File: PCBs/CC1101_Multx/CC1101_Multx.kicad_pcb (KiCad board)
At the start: 4 copper layers, 41 x 26.6 mm, 45 parts, among them IC1 CC1101RGPR, IC2 ASWD-S2-0005-T, IC3 ASWD-S2-0005-T, IC4 ASWD-S2-0005-T, J1 MCU, J2 MCU, J3 MCU, J4 MCU, J5 MCU, J6 MCU, J7 MCU, J8 MCU, J9 MCU, Y1 XRCGB26M000F1S2BR0

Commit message: layout2
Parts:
- added REF**: MountingHole_2.2mm_M2_DIN965, MountingHole:MountingHole_2.2mm_M2_DIN965, F.Cu at (152.4, 89.5)
- added REF**: MountingHole_2.2mm_M2_DIN965, MountingHole:MountingHole_2.2mm_M2_DIN965, F.Cu at (152.4, 71.5)
- added REF**: MountingHole_2.2mm_M2_DIN965, MountingHole:MountingHole_2.2mm_M2_DIN965, F.Cu at (175.1, 89.5)
- added REF**: MountingHole_2.2mm_M2_DIN965, MountingHole:MountingHole_2.2mm_M2_DIN965, F.Cu at (175.8, 71.5)
- moved BT1 2.65 mm to (159.2, 73.1)
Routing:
- net Net-(IC4-VCTL): track 45.8 -> 40.0 mm
- net Net-(IC2-VCTL): track 27.2 -> 29.2 mm
- net /AGND: track 25.7 -> 26.0 mm, vias 12 -> 119
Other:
- board size 41 x 26.6 mm -> 41.1 x 26.8 mm

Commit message: Layout V
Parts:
- moved AE1 0.12 mm to (182.2, 83.4)
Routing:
- net Net-(IC1-SCLK): track 8.63 -> 7.24 mm
- net /AGND: vias 119 -> 175

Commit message: BOM 1
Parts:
- AE1: footprint Connector_Coaxial:SMA_Molex_73251-1153_EdgeMount_Horizontal -> Connector_Coaxial:SMA_Molex_73251-2120_EdgeMount_Horizontal
- moved AE1 1.54 mm to (183.7, 83.4), turned to 0 degrees
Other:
- board size 41.1 x 26.8 mm -> 39.6 x 26.8 mm

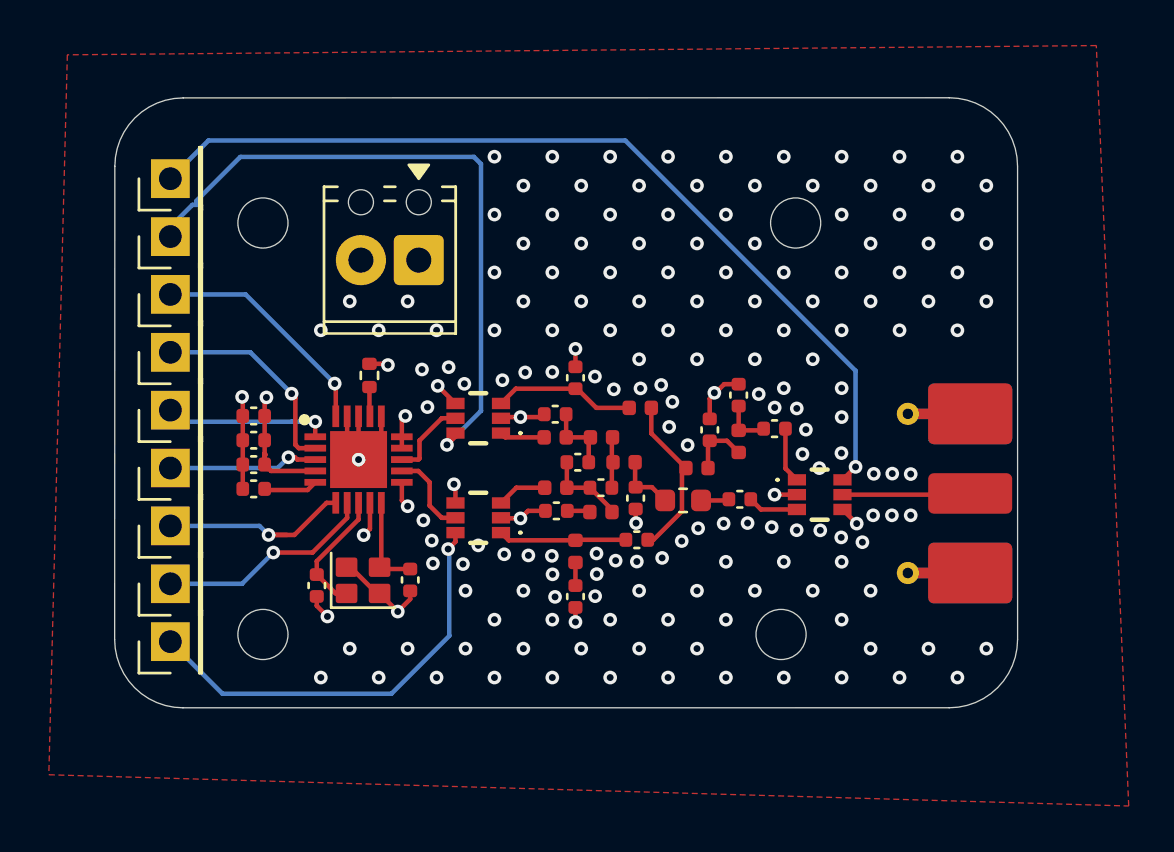
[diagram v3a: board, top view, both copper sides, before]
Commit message: Layout new switch and BOM
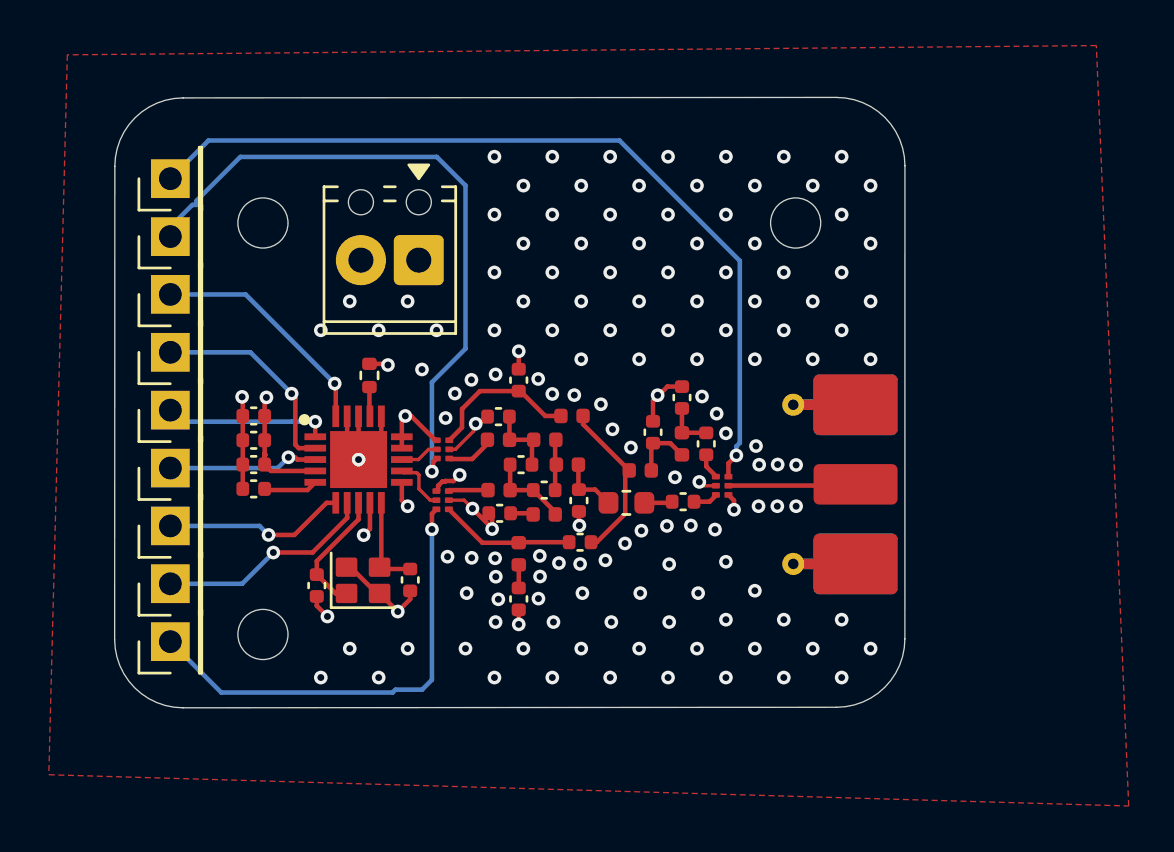
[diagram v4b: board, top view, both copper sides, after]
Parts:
- removed the REF** at (175.1, 89.5)
- C51: value 100n -> 100nF
- IC2, IC3, IC4: footprint Library:ASWDS20005T -> Library:ASWS_S2_0002
- moved AE1 5.05 mm to (178.7, 83.0)
- moved IC4 4.13 mm to (172.8, 82.6), turned to 0 degrees
- moved C125_1 3.07 mm to (171.9, 81.2), turned to 90 degrees
- moved L131_1 3.02 mm to (166.0, 80.0)
- moved IC2 2.50 mm to (160.1, 81.8), turned to 180 degrees
- moved C124_1 2.49 mm to (163.6, 88.0)
- moved C124_2 2.49 mm to (162.8, 84.2)
- moved C131_1 2.49 mm to (163.6, 78.4)
- moved L121_1 2.49 mm to (163.6, 86.0)
- moved C122_1 2.49 mm to (169.5, 80.7)
- moved C123_1 2.49 mm to (170.8, 79.2)
- moved C125_2 2.49 mm to (170.8, 83.7)
- moved C131_2 2.49 mm to (162.7, 80.0)
- moved L122_1 2.49 mm to (169.0, 82.4)
- moved L124_2 2.49 mm to (168.4, 83.8)
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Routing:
- net Net-(IC4-VCTL): track 40.0 -> 37.5 mm
- net /RF_N: track 3.56 -> 1.72 mm
- net /AGND: track 26.0 -> 27.8 mm, vias 175 -> 142
- net /RF_P: track 3.81 -> 2.40 mm
- net /433_A: track 2.45 -> 1.11 mm
- net Net-(IC3-VCTL): track 18.9 -> 20.2 mm
- net /AVDD: track 12.9 -> 14.0 mm, vias 7 -> 6
- net /868_A: track 2.21 -> 1.07 mm
- net Net-(IC1-GDO0_(ATEST)): track 8.82 -> 8.01 mm
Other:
- board size 39.6 x 26.8 mm -> 34.7 x 26.8 mm

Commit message: BOM e tudo mais
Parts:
- added REF**: MountingHole_2.2mm_M2_DIN965, MountingHole:MountingHole_2.2mm_M2_DIN965, F.Cu at (167.1, 89.5)
- moved REF** 8.64 mm to (167.1, 71.5)
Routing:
- net /AGND: vias 142 -> 139
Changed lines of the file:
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@@
 			(outputformat 1)
 			(mirror no)
-			(drillshape 1)
+			(drillshape 0)
 			(scaleselection 1)
-			(outputdirectory "")
+			(outputdirectory "Gerbers/")
 		)
 	)
@@
 		(embedded_fonts no)
 	)
+	(footprint "MountingHole:MountingHole_2.2mm_M2_DIN965"
+		(layer "F.Cu")
+		(at 167.135534 89.55)
+		(descr "Mounting Hole 2.2mm, M2, no annular, generated by kicad-footprint-generator mountinghole.py")
+		(tags "mountinghole M2 DIN965")
+		(property "Reference" "REF**"
+			(at 0 -2.85 0)
+			(layer "F.SilkS")
+			(hide yes)
+			(effects
+				(font
+					(size 1 1)
+					(thickness 0.15)
+				)
+			)
+		)
+		(property "Value" "MountingHole_2.2mm_M2_DIN965"
+			(at 0 2.85 0)
+			(layer "F.Fab")
+			(hide yes)
+			(effects
+				(font
+					(size 1 1)
+					(thickness 0.15)
+				)
+			)
+		)
+		(property "Datasheet" ""
+			(at 0 0 0)
+			(layer "F.Fab")
+			(hide yes)
+			(effects
+				(font
+					(size 1.27 1.27)
+				)
+			)
+		)
+		(property "Description" ""
+			(at 0 0 0)
+			(layer "F.Fab")
+			(hide yes)
+			(effects
+				(font
+					(size 1.27 1.27)
+				)
+			)
+		)
+		(property "KiLib_Generator" "mounting_hardware/mounting_hole"
+			(at 0 0 0)
+			(layer "F.SilkS")
+			(hide yes)
+			(effects
+				(font
+					(size 1 1)
+					(thickness 0.15)
+				)
+			)
+		)
+		(attr exclude_from_pos_files exclude_from_bom)
+		(duplicate_pad_numbers_are_jumpers no)
+		(fp_circle
+			(center 0 0)
+			(end 1.9 0)
+			(stroke
+				(width 0.15)
+				(type solid)
+			)
+			(fill no)
+			(layer "Cmts.User")
+		)
+		(fp_circle
+			(center 0 0)
+			(end 2.15 0)
+			(stroke
+				(width 0.05)
+				(type solid)
+			)
+			(fill no)
+			(layer "F.CrtYd")
+		)
+		(pad "" np_thru_hole circle
+			(at 0 0)
+			(size 2.2 2.2)
+			(drill 2.2)
+			(layers "*.Cu" "*.Mask")
+		)
+		(embedded_fonts no)
+	)
 	(footprint "Capacitor_SMD:C_0402_1005Metric"
 		(layer "F.Cu")
@@
 	(footprint "MountingHole:MountingHole_2.2mm_M2_DIN965"
 		(layer "F.Cu")
-		(at 175.78 71.49)
+		(at 167.135534 71.484449)
 		(descr "Mounting Hole 2.2mm, M2, no annular, generated by kicad-footprint-generator mountinghole.py")
 		(tags "mountinghole M2 DIN965")
@@
 	)
 	(via
+		(at 167.64 73.66)
+		(size 0.6)
+		(drill 0.3)
+		(layers "F.Cu" "B.Cu")
+		(free yes)
+		(net "/AGND")
+	)
+	(via
 		(at 161.340794 87.7359)
 		(size 0.6)
@@
 	)
 	(via
+		(at 175.26 71.12)
+		(size 0.6)
+		(drill 0.3)
+		(layers "F.Cu" "B.Cu")
+		(free yes)
+		(net "/AGND")
+	)
+	(via
 		(at 171.500794 87.7359)
 		(size 0.6)
@@
 	)
 	(via
-		(at 168.91 90.17)
-		(size 0.6)
-		(drill 0.3)
-		(layers "F.Cu" "B.Cu")
-		(free yes)
-		(net "/AGND")
-	)
-	(via
 		(at 175.800792 82.1107)
 		(size 0.6)
@@
 	)
 	(via
+		(at 165.1 73.66)
+		(size 0.6)
+		(drill 0.3)
+		(layers "F.Cu" "B.Cu")
+		(free yes)
+		(net "/AGND")
+	)
+	(via
 		(at 173.99 72.39)
 		(size 0.6)
@@
 	)
 	(via
-		(at 165.150794 89.0059)
+		(at 176.53 72.39)
 		(size 0.6)
 		(drill 0.3)
@@
 	)
 	(via
-		(at 165.1 71.12)
-		(size 0.6)
-		(drill 0.3)
-		(layers "F.Cu" "B.Cu")
-		(net "/AGND")
-	)
-	(via
 		(at 167.64 76.2)
 		(size 0.6)
@@
 	)
 	(via
-		(at 168.91 72.39)
+		(at 177.8 88.9)
 		(size 0.6)
 		(drill 0.3)
 		(layers "F.Cu" "B.Cu")
+		(free yes)
 		(net "/AGND")
 	)
 	(via
-		(at 177.8 88.9)
+		(at 165.1 71.12)
 		(size 0.6)
 		(drill 0.3)
@@
 	)
 	(via
-		(at 167.64 73.66)
+		(at 161.29 90.17)
 		(size 0.6)
 		(drill 0.3)
 		(layers "F.Cu" "B.Cu")
+		(free yes)
 		(net "/AGND")
 	)
 	(via
-		(at 161.29 90.17)
+		(at 158.75 90.17)
 		(size 0.6)
 		(drill 0.3)
@@
 	)
 	(via
-		(at 158.75 90.17)
+		(at 173.99 87.63)
 		(size 0.6)
 		(drill 0.3)
@@
 	)
 	(via
-		(at 173.99 87.63)
+		(at 168.91 72.39)
 		(size 0.6)
 		(drill 0.3)
@@
 	)
 	(via
+		(at 166.37 74.93)
+		(size 0.6)
+		(drill 0.3)
+		(layers "F.Cu" "B.Cu")
+		(free yes)
+		(net "/AGND")
+	)
+	(via
 		(at 171.45 74.93)
 		(size 0.6)
@@
 	)
 	(via
-		(at 166.37 90.17)
+		(at 166.37 69.85)
 		(size 0.6)
 		(drill 0.3)
@@
 	)
 	(via
-		(at 173.99 77.47)
+		(at 166.37 87.63)
 		(size 0.6)
 		(drill 0.3)
@@
 	)
 	(via
-		(at 159.38 77.92)
-		(size 0.6)
-		(drill 0.3)
-		(layers "F.Cu" "B.Cu")
-		(net "/AGND")
-	)
-	(via
-		(at 169.010794 84.9959)
-		(size 0.6)
-		(drill 0.3)
-		(layers "F.Cu" "B.Cu")
-		(net "/AGND")
-	)
-	(via
-		(at 172.72 76.2)
+		(at 173.99 77.47)
 		(size 0.6)
 		(drill 0.3)
 		(layers "F.Cu" "B.Cu")
+		(free yes)
 		(net "/AGND")
 	)
 	(via
-		(at 165.1 73.66)
+		(at 159.38 77.92)
 		(size 0.6)
 		(drill 0.3)
@@
 	)
 	(via
-		(at 166.37 72.39)
+		(at 169.010794 84.9959)
 		(size 0.6)
 		(drill 0.3)
@@
 	)
 	(via
-		(at 166.420794 87.7359)
+		(at 172.72 76.2)
 		(size 0.6)
 		(drill 0.3)
 		(layers "F.Cu" "B.Cu")
-		(free yes)
 		(net "/AGND")
 	)
@@
 	)
 	(via
-		(at 167.690794 89.0059)
-		(size 0.6)
-		(drill 0.3)
-		(layers "F.Cu" "B.Cu")
-		(free yes)
-		(net "/AGND")
-	)
-	(via
 		(at 157.48 91.44)
 		(size 0.6)
@@
 	)
 	(via
-		(at 167.64 71.12)
-		(size 0.6)
-		(drill 0.3)
-		(layers "F.Cu" "B.Cu")
-		(net "/AGND")
-	)
-	(via
 		(at 162.56 91.44)
 		(size 0.6)
@@
 	)
 	(via
-		(at 166.37 69.85)
-		(size 0.6)
-		(drill 0.3)
-		(layers "F.Cu" "B.Cu")
-		(net "/AGND")
-	)
-	(via
-		(at 166.37 74.93)
-		(size 0.6)
-		(drill 0.3)
-		(layers "F.Cu" "B.Cu")
-		(net "/AGND")
-	)
-	(via
 		(at 162.610794 78.1359)
 		(size 0.6)
@@
 		(size 0.6)
 		(drill 0.3)
+		(layers "F.Cu" "B.Cu")
+		(free yes)
+		(net "/AGND")
+	)
+	(via
+		(at 168.91 90.17)
+		(size 0.6)
+		(drill 0.3)

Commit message: V3 Fasivel
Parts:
- removed IC2, IC3, IC4: ASWD-S2-0005-T, Library:ASWS_S2_0002
- removed the REF** at (167.1, 89.5)
- removed the REF** at (167.1, 71.5)
- added J1: MCU, Connector_PinHeader_2.54mm:PinHeader_1x01_P2.54mm_Vertical, F.Cu at (145.6, 76.1)
- added REF**: MountingHole_2.2mm_M2_DIN965, MountingHole:MountingHole_2.2mm_M2_DIN965, F.Cu at (177.6, 71.5)
- added REF**: MountingHole_2.2mm_M2_DIN965, MountingHole:MountingHole_2.2mm_M2_DIN965, F.Cu at (177.6, 89.6)
- added U1: 4259-63, Library:SC-70-6_PSM-M, F.Cu at (161.6, 80.6)
- added U2: 4259-63, Library:SC-70-6_PSM-M, F.Cu at (176.8, 83.0)
- added U3: 4259-63, Library:SC-70-6_PSM-M, F.Cu at (161.6, 83.8)
- AE1: footprint Connector_Coaxial:SMA_Molex_73251-2120_EdgeMount_Horizontal -> Library:SMA_CONSMA020_062_G
- BT1: footprint TerminalBlock_Phoenix:TerminalBlock_Phoenix_MPT-0,5-2-2.54_1x02_P2.54mm_Horizontal -> Connector_PinHeader_2.54mm:PinHeader_1x02_P2.54mm_Vertical
- moved BT1 11.1 mm to (148.2, 73.6), turned to -90 degrees
- moved J2 9.51 mm to (145.6, 86.3)
- moved J9 9.51 mm to (145.6, 78.7)
- moved J4 9.51 mm to (145.6, 83.8)
- moved J7 9.51 mm to (145.6, 81.2)
- moved AE1 5.24 mm to (183.9, 83.0)
- moved J1 3.58 mm to (148.2, 76.1)
- moved J5 3.58 mm to (148.2, 81.2)
- moved J3 3.58 mm to (148.2, 78.7)
- moved J6 3.58 mm to (148.2, 83.8)
- moved J8 3.58 mm to (148.2, 86.3)
- moved C125_1 2.15 mm to (174.0, 81.5)
- moved C125_2 2.13 mm to (173.0, 83.7)
- moved C123_1 2.13 mm to (172.9, 79.2)
- moved C124_1 2.13 mm to (165.8, 88.0)
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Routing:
- net Net-(J9-Pin_1): track 37.5 -> 51.8 mm, vias 1 -> 2
- net Net-(IC1-SO_(GDO1)): track 9.32 -> 18.7 mm
- net Net-(J7-Pin_1): track 29.0 -> 35.8 mm
- net Net-(J8-Pin_1): track 20.2 -> 26.1 mm
- net Net-(IC1-SI): track 10.3 -> 14.5 mm
- net Net-(IC1-GDO2): track 6.60 -> 9.53 mm, vias 1 -> 0
- net Net-(IC1-SCLK): track 7.24 -> 9.77 mm, vias 1 -> 0
- net Net-(IC1-GDO0_(ATEST)): track 8.01 -> 9.74 mm, vias 1 -> 0
- net /RF_N: track 1.72 -> 3.14 mm
- net /868_A: track 1.07 -> 2.20 mm
- net /433_N: track 6.71 -> 5.72 mm
- net /433_A: track 1.11 -> 1.94 mm
- net /RF_P: track 2.40 -> 3.16 mm
- net /To_Ant: track 6.18 -> 6.91 mm
- net /AVDD: track 14.0 -> 13.4 mm
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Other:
- board size 34.7 x 26.8 mm -> 43.7 x 25.9 mm
- board text added: "Made By: F.Lima"

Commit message: 2ants prod
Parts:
- removed U2: 4259-63, Library:SC-70-6_PSM-M
- added AE2: Antenna_Shield, Library:SMA_CONSMA020_062_G, F.Cu at (175.6, 86.0)
- moved AE1 12.4 mm to (175.6, 73.7)
- moved C125_1 7.70 mm to (171.6, 74.2), turned to -90 degrees
- moved REF** 6.86 mm to (170.8, 71.4)
- moved REF** 6.86 mm to (170.8, 89.5)
- moved C123_1 3.35 mm to (171.1, 76.3), turned to 0 degrees
- moved L123_1 3.00 mm to (171.6, 78.5)
- moved C125_2 2.54 mm to (171.3, 85.6), turned to 90 degrees
- moved C122_1 0.55 mm to (171.1, 80.7), turned to 0 degrees
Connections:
- AE1 pad 1: /To_Ant -> /433_A
- J9 pad 1: Net-(J9-Pin_1) -> /AGND
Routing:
- net Net-(J9-Pin_1): track 51.8 -> 0.00 mm, vias 2 -> 0
- net /To_Ant: track 6.91 -> 0.00 mm
- net Net-(J7-Pin_1): track 35.8 -> 32.0 mm
- net /AGND: track 28.4 -> 24.8 mm, vias 195 -> 144
- net /868_A: track 2.20 -> 4.38 mm
- net /433_A: track 1.94 -> 4.05 mm
- net /AVDD: track 13.0 -> 11.8 mm, vias 6 -> 5
- net Net-(C123_1-Pad2): track 2.36 -> 3.33 mm
- net Net-(C122_1-Pad2): track 2.71 -> 3.37 mm
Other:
- board size 43.7 x 25.9 mm -> 35.4 x 25.9 mm
